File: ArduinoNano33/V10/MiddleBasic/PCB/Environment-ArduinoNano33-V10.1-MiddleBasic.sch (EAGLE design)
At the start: 4 parts

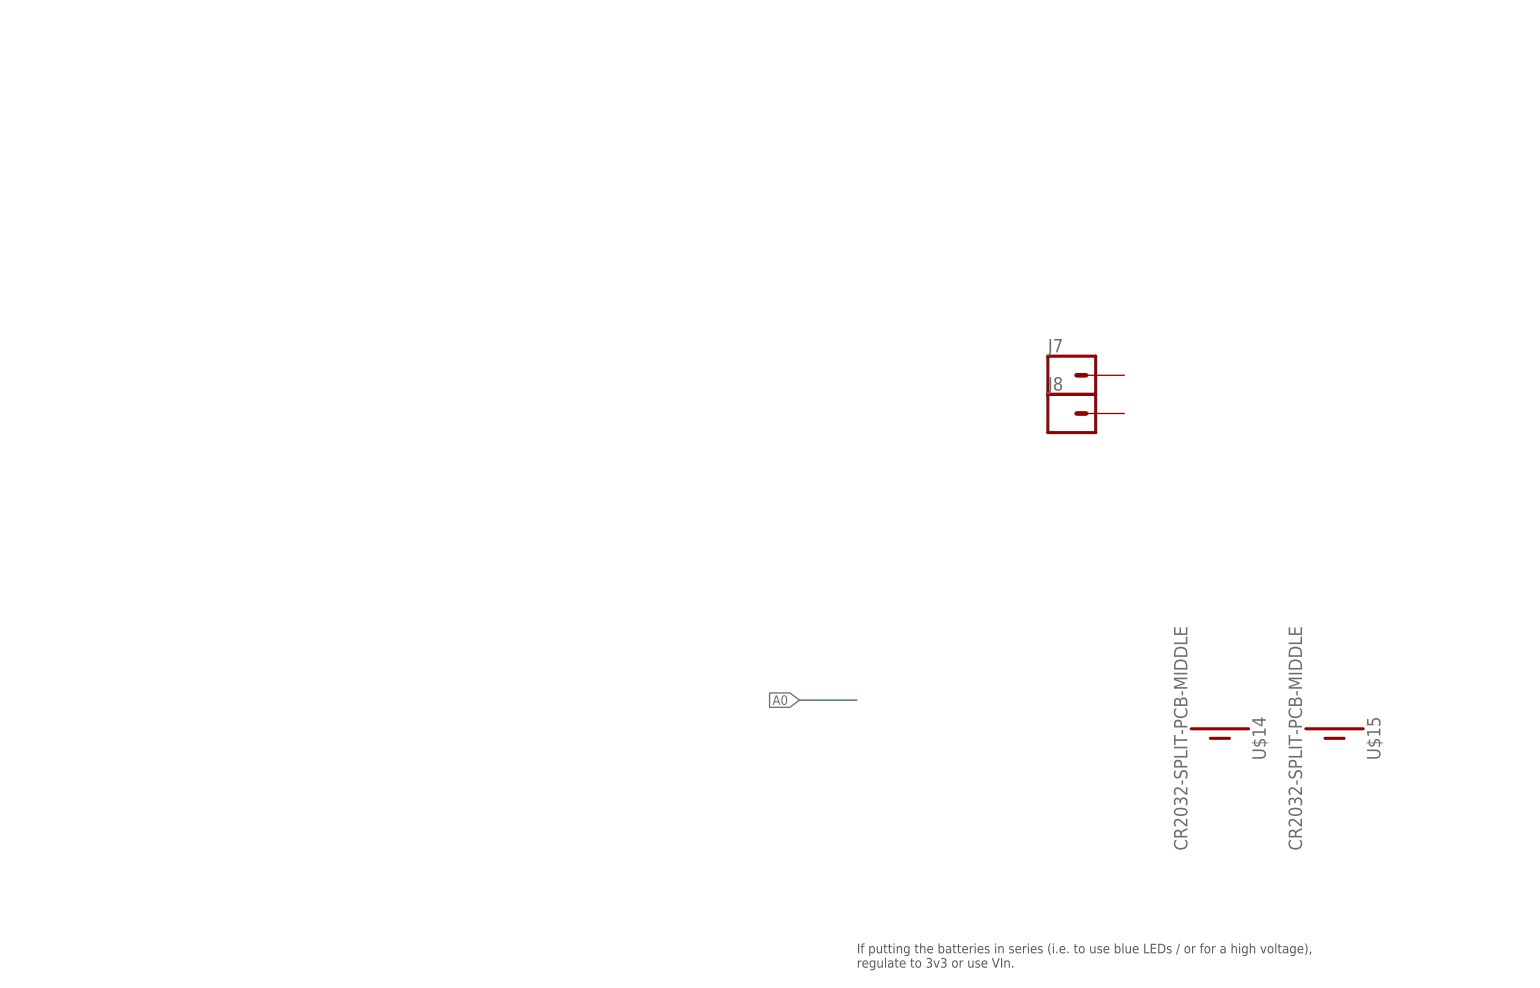
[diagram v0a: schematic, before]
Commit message: Update for V10.1 with improvements...
* Removed USB C until I get a better foot print for the ones I can buy and replaced with Micro B
* Reduced cutout in middle layers as it doesn't need so much space.
* Increased hole size in middle layers for potential NFC wire passthrough to prevent clashes with solder
* Added potential extra solder connection for bottom to middle layers.
* Changed bottom boards so they use a top side pad to be soldered to rather than a hole to make the bottom face tidier.
* Removed switch on the top board as it would have been weird to use
* Added potential divider for the "3v3" supply to allow monitoring of battery voltage (although this may drain the battery too much)
* Extended the pads (where possible) for the Arduino to make hand soldering it to the board easier.
* Improved top level silk screen text
* Added "Up" to the bottom/middle layers to aid assembly.
* Fixed issue with missing holes on the non-key chain middle layer.
* Improved custom bottoms to be one PCB per customisation
* General tidy up of the reference lines
* Improved (fixed!) some of the filenames

Sent to JLCPCB - 27 Feb 2020
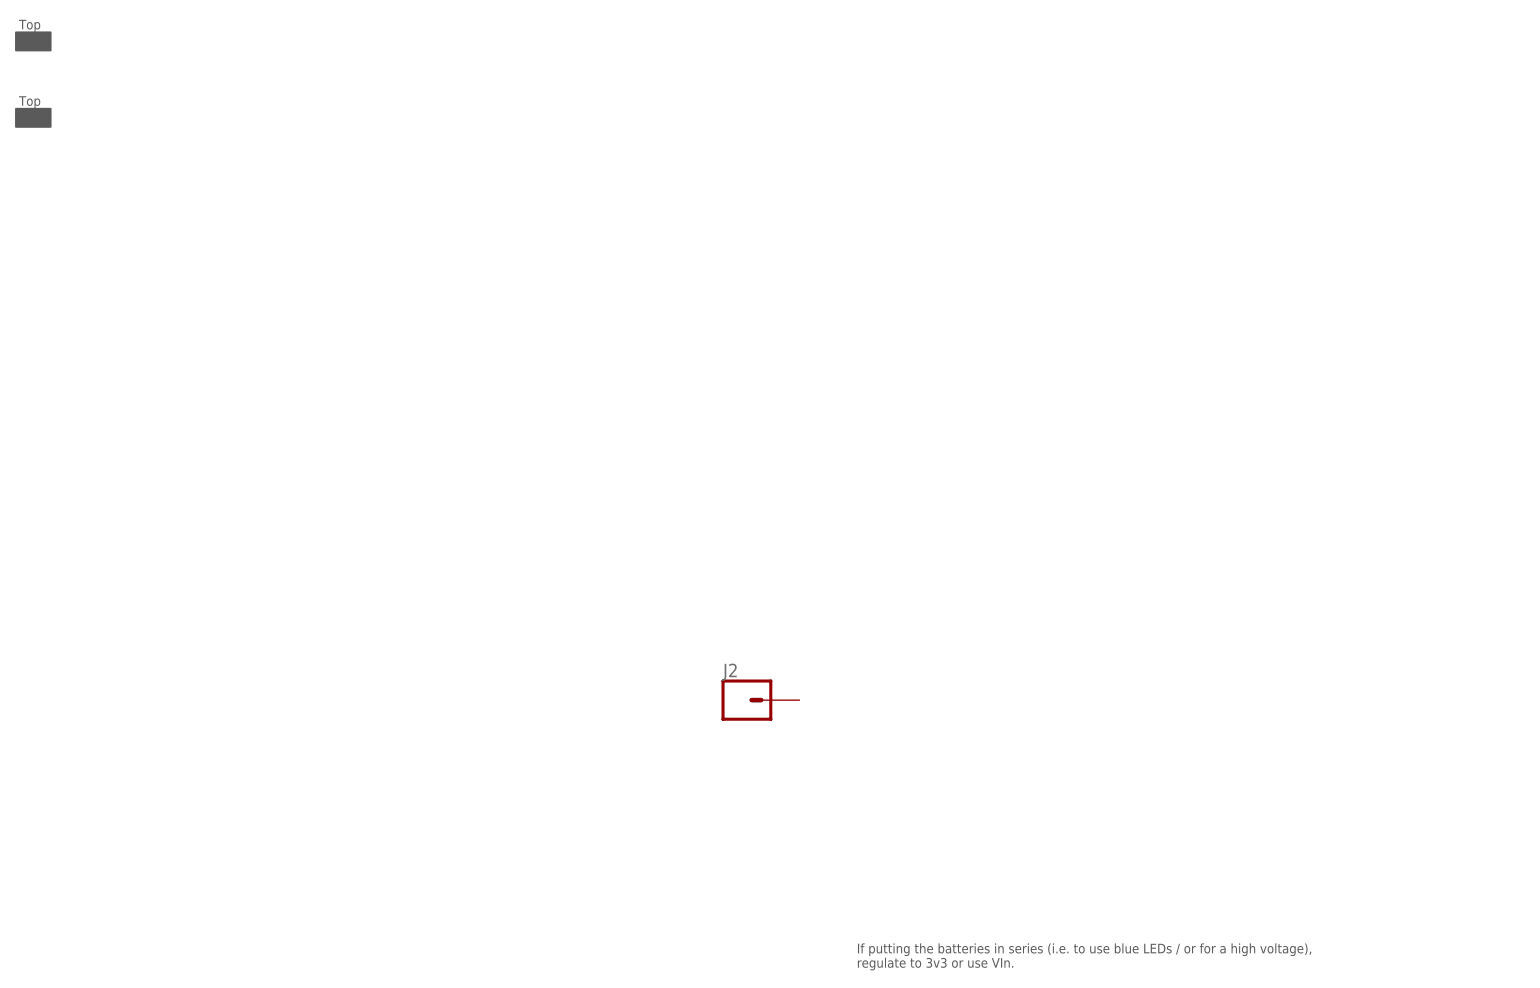
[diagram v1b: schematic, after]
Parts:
- removed J7, J8: (no value), SparkFun-Connectors:CONN_01
- removed U$14, U$15: CR2032-SPLIT-PCB-MIDDLE, ThingySticks:CR2032-SPLIT-PCB-MIDDLE
- added J2: (no value), SparkFun-Connectors:CONN_01
- added U$1: PERSONAL_ENVIRONMENT_SENSORBOTTOM, ThingySticks:PERSONAL_ENVIRONMENT_SENSORBOTTOM
- added U$2: PERSONAL_ENVIRONMENT_SENSORTOP, ThingySticks:PERSONAL_ENVIRONMENT_SENSORTOP
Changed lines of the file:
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@@
 <parts>
 <part name="FRAME1" library="SparkFun-Aesthetics" deviceset="FRAME-A4L" device=""/>
-<part name="U$14" library="ThingySticks" deviceset="CR2032-SPLIT-PCB-MIDDLE" device=""/>
-<part name="U$15" library="ThingySticks" deviceset="CR2032-SPLIT-PCB-MIDDLE" device=""/>
-<part name="J7" library="SparkFun-Connectors" deviceset="CONN_01" device=""/>
-<part name="J8" library="SparkFun-Connectors" deviceset="CONN_01" device=""/>
+<part name="J2" library="SparkFun-Connectors" deviceset="CONN_01" device=""/>
+<part name="U$1" library="ThingySticks" deviceset="PERSONAL_ENVIRONMENT_SENSOR" device="BOTTOM"/>
+<part name="U$2" library="ThingySticks" deviceset="PERSONAL_ENVIRONMENT_SENSOR" device="TOP"/>
 </parts>
 <sheets>
@@
 <instances>
 <instance part="FRAME1" gate="G$1" x="-96.52" y="-17.78"/>
-<instance part="U$14" gate="G$1" x="134.62" y="38.1" rot="R270"/>
-<instance part="U$15" gate="G$1" x="149.86" y="38.1" rot="R270"/>
-<instance part="J7" gate="G$1" x="114.3" y="86.36"/>
-<instance part="J8" gate="G$1" x="114.3" y="81.28"/>
+<instance part="J2" gate="G$1" x="71.12" y="43.18"/>
+<instance part="U$1" gate="G$1" x="-25.4" y="119.38"/>
+<instance part="U$2" gate="G$1" x="-25.4" y="129.54"/>
 </instances>
 <busses>
 </busses>
 <nets>
-<net name="A0" class="0">
-<segment>
-<wire x1="86.36" y1="43.18" x2="78.74" y2="43.18" width="0.1524" layer="91"/>
-<label x="78.74" y="43.18" size="1.27" layer="95" rot="R180" xref="yes"/>
-</segment>
-</net>
 </nets>
 </sheet>
 </sheets>
-<errors>
-</errors>
 </schematic>
 </drawing>
